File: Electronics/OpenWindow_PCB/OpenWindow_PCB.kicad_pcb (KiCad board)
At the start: 2 copper layers, 65 x 70 mm, 46 parts, among them J1 Door connector, J2 C2 connector, J3 FTDI connector, J4 Relay Connector 2, J5 ACS712 PCB Connector, J6 Relay Connector 1, Q1 FQU17P06TU, Q2 2N7000, Q3 FQU17P06TU, Q4 PN2222A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

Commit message: Added PCB layout output files
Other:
- board text added: "JLCJLCJLCJLC"

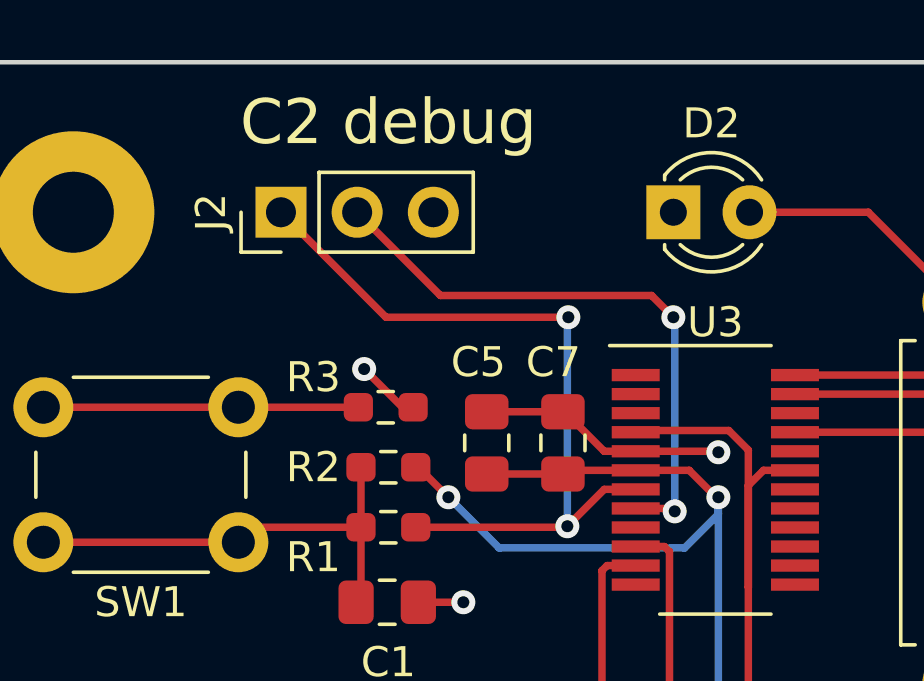
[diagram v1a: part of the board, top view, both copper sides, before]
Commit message: Corrected C2 debug header
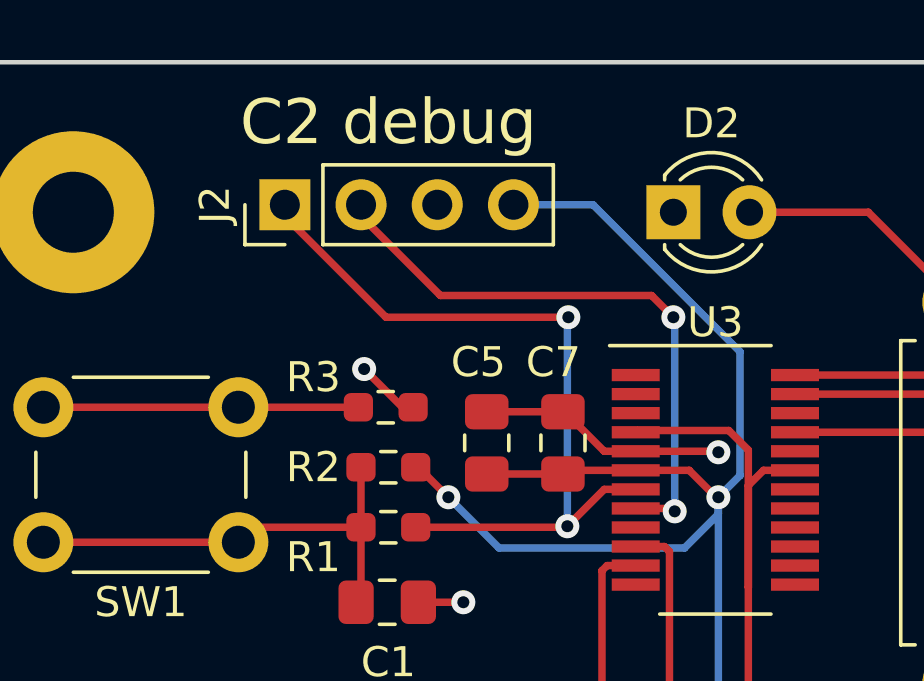
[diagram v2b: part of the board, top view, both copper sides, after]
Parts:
- J2: value C2 connector -> C2 debug; footprint Connector_PinHeader_2.54mm:PinHeader_1x03_P2.54mm_Vertical -> Connector_PinHeader_2.54mm:PinHeader_1x04_P2.54mm_Vertical
- moved J2 0.28 mm to (62.0, 34.8)
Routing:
- net +3V3: track 52.9 -> 67.6 mm
